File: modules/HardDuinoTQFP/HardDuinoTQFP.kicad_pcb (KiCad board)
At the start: 2 copper layers, 40.6 x 40.6 mm, 21 parts, among them J1 Conn_01x10_Male, J2 Conn_01x10_Male, J3 Conn_01x05_Male, J4 Conn_02x03_Odd_Even, U1 ATmega328P-AU, Y1 16MHz

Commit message: HardDuinoTQFP. Add photomask & hash
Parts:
- added J5: Conn_01x01_Male, Connector_PinHeader_2.54mm:PinHeader_1x01_P2.54mm_Vertical, F.Cu at (114.3, 75.9)
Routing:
- net Net-(C2-Pad1): track 10.4 -> 13.9 mm
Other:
- board text added: "2effdf"
- board text added: "31.05.2020"
- board text removed: "16.05.2020"
- board text removed: "6882a8"
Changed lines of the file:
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@@
     (thickness 1.6)
     (drawings 40)
-    (tracks 287)
+    (tracks 289)
     (zones 0)
-    (modules 21)
+    (modules 22)
     (nets 32)
   )
@@
   )
   (setup
-    (last_trace_width 0.5)
+    (last_trace_width 0.25)
     (user_trace_width 0.4)
     (user_trace_width 0.5)
@@
     )
   )
+  (module Connector_PinHeader_2.54mm:PinHeader_1x01_P2.54mm_Vertical (layer F.Cu)
+    (at 114.3 75.8825)
+    (descr "Through hole straight pin header, 1x01, 2.54mm pitch, single row")
+    (tags "Through hole pin header THT 1x01 2.54mm single row")
+    (fp_text reference J5 (at 0 -2.33) (layer F.SilkS)
+      (effects (font (size 1 1) (thickness 0.15)))
+    )
+    (fp_text value Conn_01x01_Male (at 0 2.33) (layer F.Fab)
+      (effects (font (size 1 1) (thickness 0.15)))
+    )
+    (fp_line (start -0.635 -1.27) (end 1.27 -1.27) (layer F.Fab) (width 0.1))
+    (fp_line (start 1.27 -1.27) (end 1.27 1.27) (layer F.Fab) (width 0.1))
+    (fp_line (start 1.27 1.27) (end -1.27 1.27) (layer F.Fab) (width 0.1))
+    (fp_line (start -1.27 1.27) (end -1.27 -0.635) (layer F.Fab) (width 0.1))
+    (fp_line (start -1.27 -0.635) (end -0.635 -1.27) (layer F.Fab) (width 0.1))
+    (fp_line (start -1.33 1.33) (end 1.33 1.33) (layer F.SilkS) (width 0.12))
+    (fp_line (start -1.33 1.27) (end -1.33 1.33) (layer F.SilkS) (width 0.12))
+    (fp_line (start 1.33 1.27) (end 1.33 1.33) (layer F.SilkS) (width 0.12))
+    (fp_line (start -1.33 1.27) (end 1.33 1.27) (layer F.SilkS) (width 0.12))
+    (fp_line (start -1.33 0) (end -1.33 -1.33) (layer F.SilkS) (width 0.12))
+    (fp_line (start -1.33 -1.33) (end 0 -1.33) (layer F.SilkS) (width 0.12))
+    (fp_line (start -1.8 -1.8) (end -1.8 1.8) (layer F.CrtYd) (width 0.05))
+    (fp_line (start -1.8 1.8) (end 1.8 1.8) (layer F.CrtYd) (width 0.05))
+    (fp_line (start 1.8 1.8) (end 1.8 -1.8) (layer F.CrtYd) (width 0.05))
+    (fp_line (start 1.8 -1.8) (end -1.8 -1.8) (layer F.CrtYd) (width 0.05))
+    (fp_text user %R (at 0 0 90) (layer F.Fab)
+      (effects (font (size 1 1) (thickness 0.15)))
+    )
+    (pad 1 thru_hole rect (at 0 0) (size 1.7 1.7) (drill 1) (layers *.Cu *.Mask)
+      (net 22 "Net-(C2-Pad1)"))
+    (model ${KISYS3DMOD}/Connector_PinHeader_2.54mm.3dshapes/PinHeader_1x01_P2.54mm_Vertical.wrl
+      (at (xyz 0 0 0))
+      (scale (xyz 1 1 1))
+      (rotate (xyz 0 0 0))
+    )
+  )
   (gr_text ISP (at 103.505 46.355) (layer F.SilkS)
     (effects (font (size 1.5 1.5) (thickness 0.25)))
@@
     (effects (font (size 1 1) (thickness 0.15)))
   )
-  (gr_text 6882a8 (at 118.745 75.565) (layer F.Cu)
+  (gr_text 2effdf (at 118.745 75.565) (layer F.Cu)
     (effects (font (size 1 1) (thickness 0.2)))
   )
@@
     (effects (font (size 1.5 1.5) (thickness 0.3)))
   )
-  (gr_text 16.05.2020 (at 118.11 77.47) (layer F.Cu)
+  (gr_text 31.05.2020 (at 118.11 77.7875) (layer F.Cu)
     (effects (font (size 1 1) (thickness 0.2)))
   )
@@
   (segment (start 98.67 70.875) (end 100.33 70.875) (width 0.5) (layer B.Cu) (net 21))
   (segment (start 95.25 70.875) (end 98.67 70.875) (width 0.5) (layer B.Cu) (net 21))
-  (segment (start 104.97 59.455) (end 99.93 59.455) (width 0.5) (layer F.Cu) (net 31))
-  (segment (start 99.93 59.455) (end 99.695 59.69) (width 0.5) (layer F.Cu) (net 31))
-  (segment (start 99.695 59.69) (end 99.695 60.96) (width 0.5) (layer F.Cu) (net 31))
-  (segment (start 99.695 60.96) (end 97.79 62.865) (width 0.5) (layer F.Cu) (net 31))
-  (segment (start 97.79 62.865) (end 97.79 64.4525) (width 0.5) (layer F.Cu) (net 31))
-  (segment (start 97.79 64.4525) (end 97.79 68.8975) (width 0.5) (layer F.Cu) (net 31))
-  (segment (start 104.3125 68.875) (end 104.29 68.8975) (width 0.5) (layer B.Cu) (net 31))
   (segment (start 114.210216 72.479784) (end 113.03 71.299568) (width 0.5) (layer B.Cu) (net 22))
   (segment (start 113.03 71.299568) (end 113.03 69.85) (width 0.5) (layer B.Cu) (net 22))
@@
   (segment (start 111.76 68.58) (end 111.76 67.31) (width 0.5) (layer B.Cu) (net 22))
   (segment (start 113.03 69.85) (end 111.76 68.58) (width 0.5) (layer B.Cu) (net 22))
+  (segment (start 114.210216 75.792716) (end 114.3 75.8825) (width 0.5) (layer B.Cu) (net 22))
+  (segment (start 114.210216 72.479784) (end 114.210216 75.792716) (width 0.5) (layer B.Cu) (net 22))
   (segment (start 118.013887 66.399319) (end 116.480681 66.399319) (width 0.5) (layer B.Cu) (net 23))
   (segment (start 119.152284 67.537716) (end 118.013887 66.399319) (width 0.5) (layer B.Cu) (net 23))
@@
   (segment (start 100.71363 63.745) (end 100.6475 63.67887) (width 0.5) (layer B.Cu) (net 28))
   (segment (start 102.87 63.745) (end 100.71363 63.745) (width 0.5) (layer B.Cu) (net 28))
+  (segment (start 104.97 59.455) (end 99.93 59.455) (width 0.5) (layer F.Cu) (net 31))
+  (segment (start 99.93 59.455) (end 99.695 59.69) (width 0.5) (layer F.Cu) (net 31))
+  (segment (start 99.695 59.69) (end 99.695 60.96) (width 0.5) (layer F.Cu) (net 31))
+  (segment (start 99.695 60.96) (end 97.79 62.865) (width 0.5) (layer F.Cu) (net 31))
+  (segment (start 97.79 62.865) (end 97.79 64.4525) (width 0.5) (layer F.Cu) (net 31))
+  (segment (start 97.79 64.4525) (end 97.79 68.8975) (width 0.5) (layer F.Cu) (net 31))
+  (segment (start 104.3125 68.875) (end 104.29 68.8975) (width 0.5) (layer B.Cu) (net 31))
   (segment (start 106.045 46.6725) (end 106.045 43.18) (width 0.5) (layer B.Cu) (net 31))
   (segment (start 97.4725 56.515) (end 101.6 52.3875) (width 0.5) (layer B.Cu) (net 31))

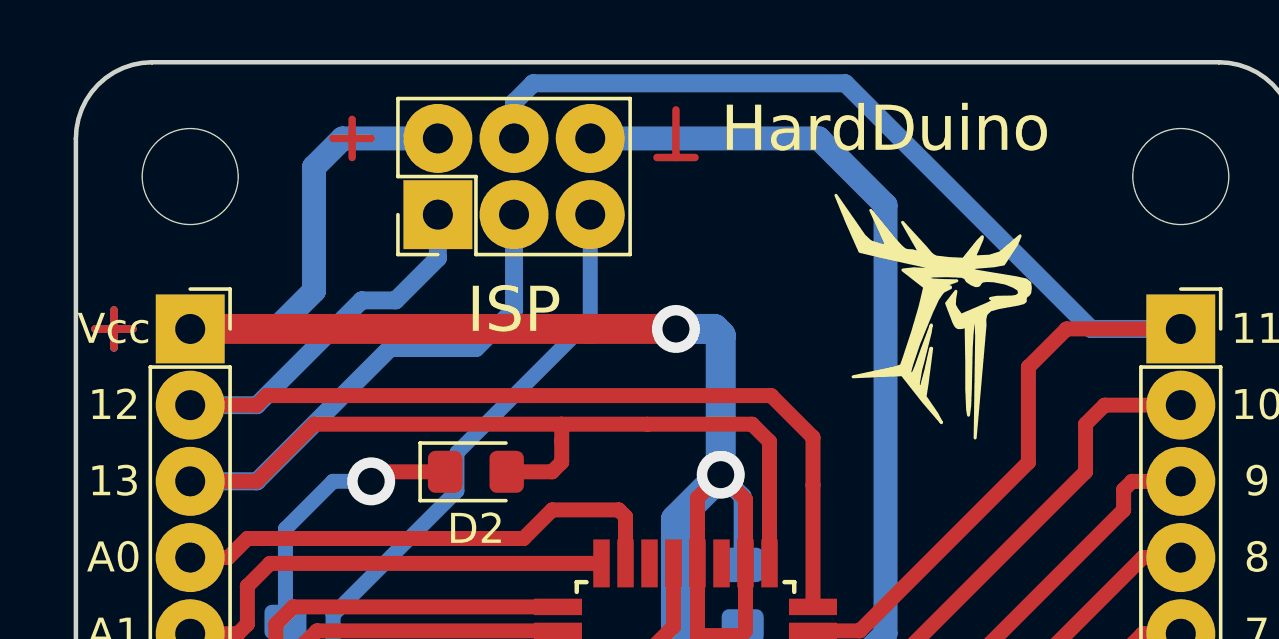
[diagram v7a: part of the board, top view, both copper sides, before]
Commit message: HardDuinoTQFP: add protection, remove AREF
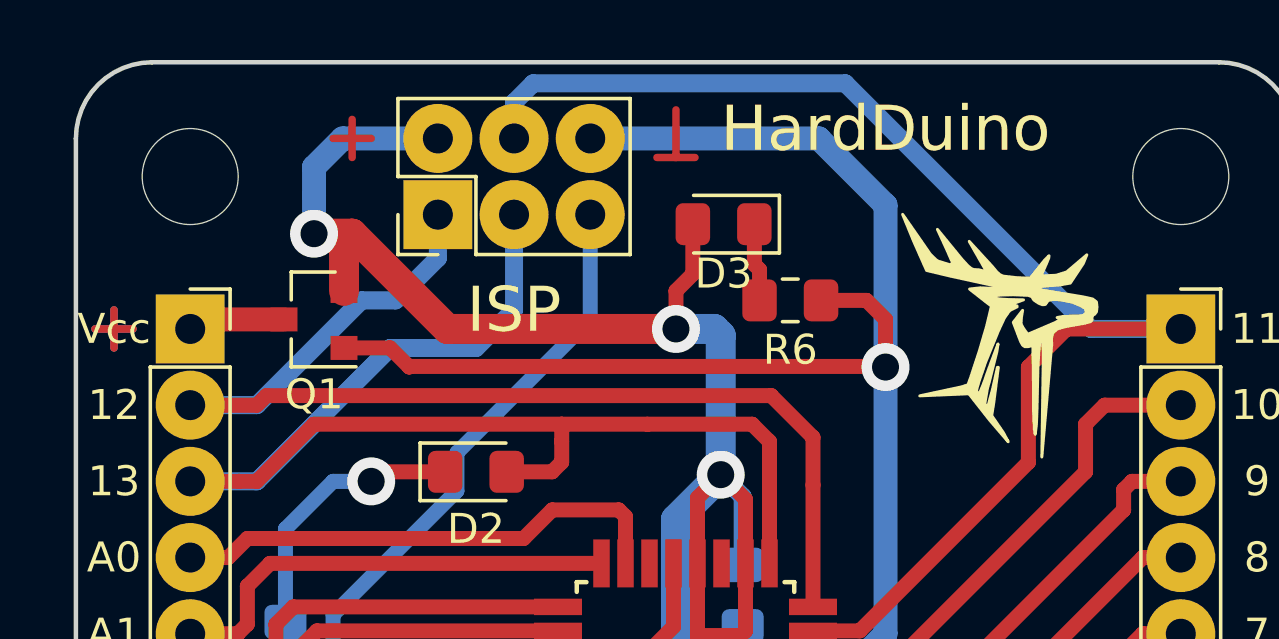
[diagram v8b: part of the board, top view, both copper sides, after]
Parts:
- added D3: LED, LED_SMD:LED_0805_2012Metric_Pad1.15x1.40mm_HandSolder, F.Cu at (110.5, 43.5)
- added Q1: IRLML5203, Package_TO_SOT_SMD:SOT-23, F.Cu at (96.8, 46.7)
- added R6: 1k, Resistor_SMD:R_0805_2012Metric_Pad1.15x1.40mm_HandSolder, F.Cu at (112.7, 46.0)
- C4: value C -> 0.1uF
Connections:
- J1 pad 1: VCC -> Net-(J1-Pad1)
- U1 pad 20: VCC -> Net-(U1-Pad20)
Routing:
- net GND: track 110.8 -> 133.1 mm, vias 1 -> 2
- net VCC: track 89.8 -> 86.2 mm, vias 2 -> 3
- net Net-(J1-Pad1): track 0.00 -> 3.26 mm
- net Net-(D3-Pad1): track 0.00 -> 2.61 mm
